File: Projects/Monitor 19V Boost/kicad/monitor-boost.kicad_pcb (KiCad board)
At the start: 2 copper layers, 148 x 118 mm, 47 parts, among them J1 12V IN, J2 19V OUT, Q1 P36NF06, Q2 BD139, Q3 BD140, U1 SG3524

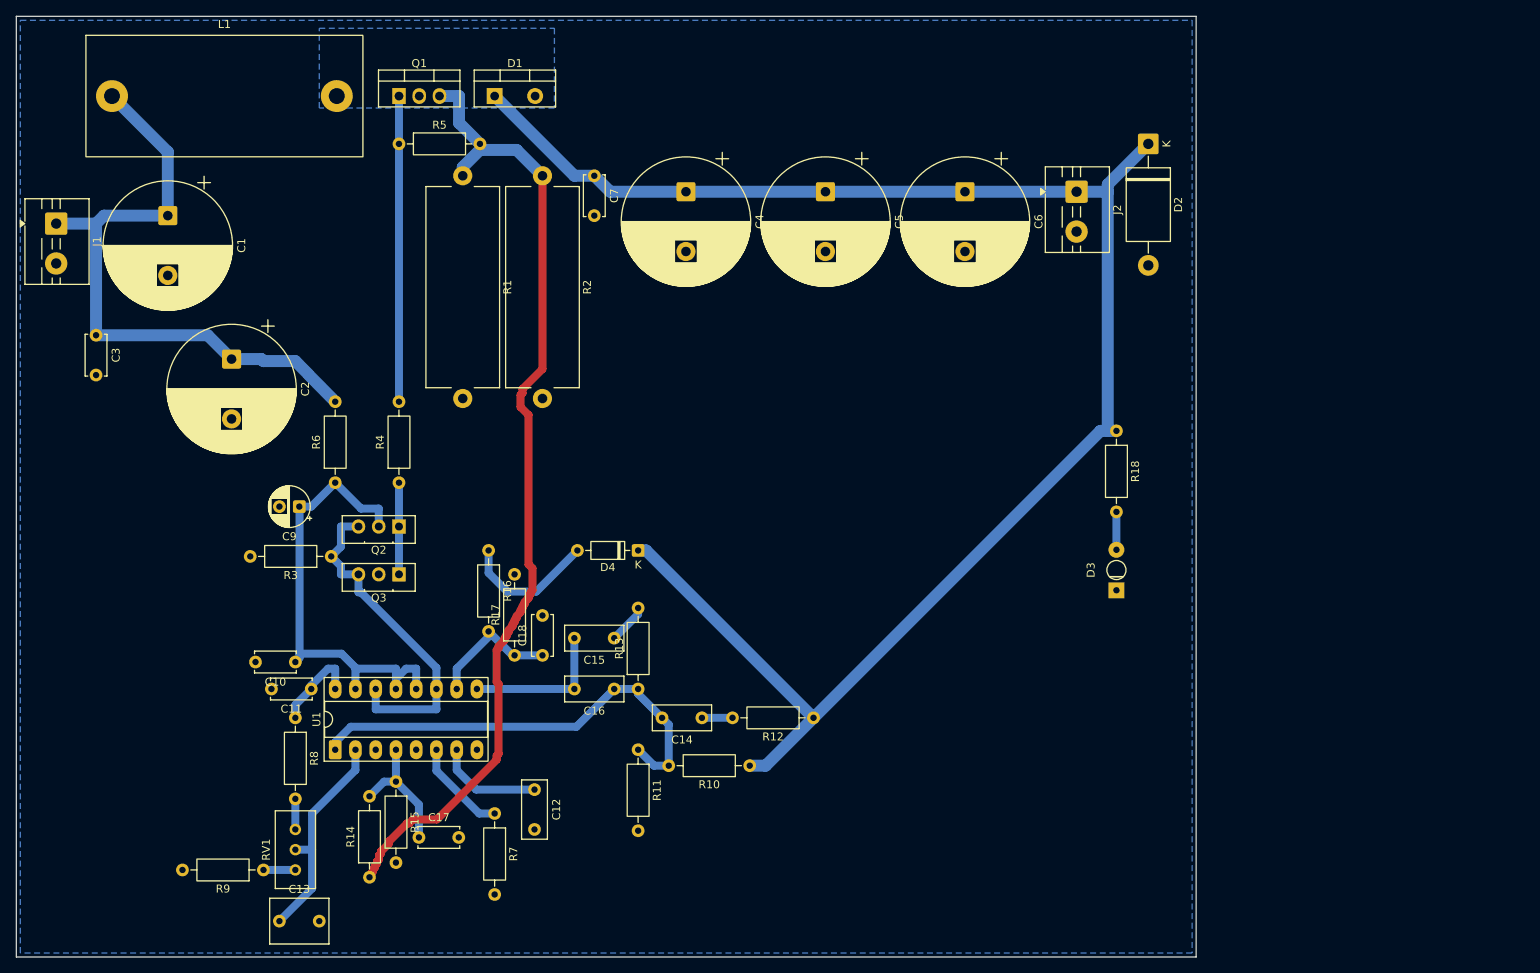
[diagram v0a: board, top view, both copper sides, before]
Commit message: Monitor 19V Boost: hand-drawn layout (before ground fix)
Mads's own redraw of the board. Routes fully on B.Cu with no wire links,
but the VOUT and CS tracks wall the output caps' ground off from the
shunt (hot-loop return ~250 mm round the board edge) and the +12V track
splits C1's minus from the shunt. Kept as the reference for the fix that
follows.
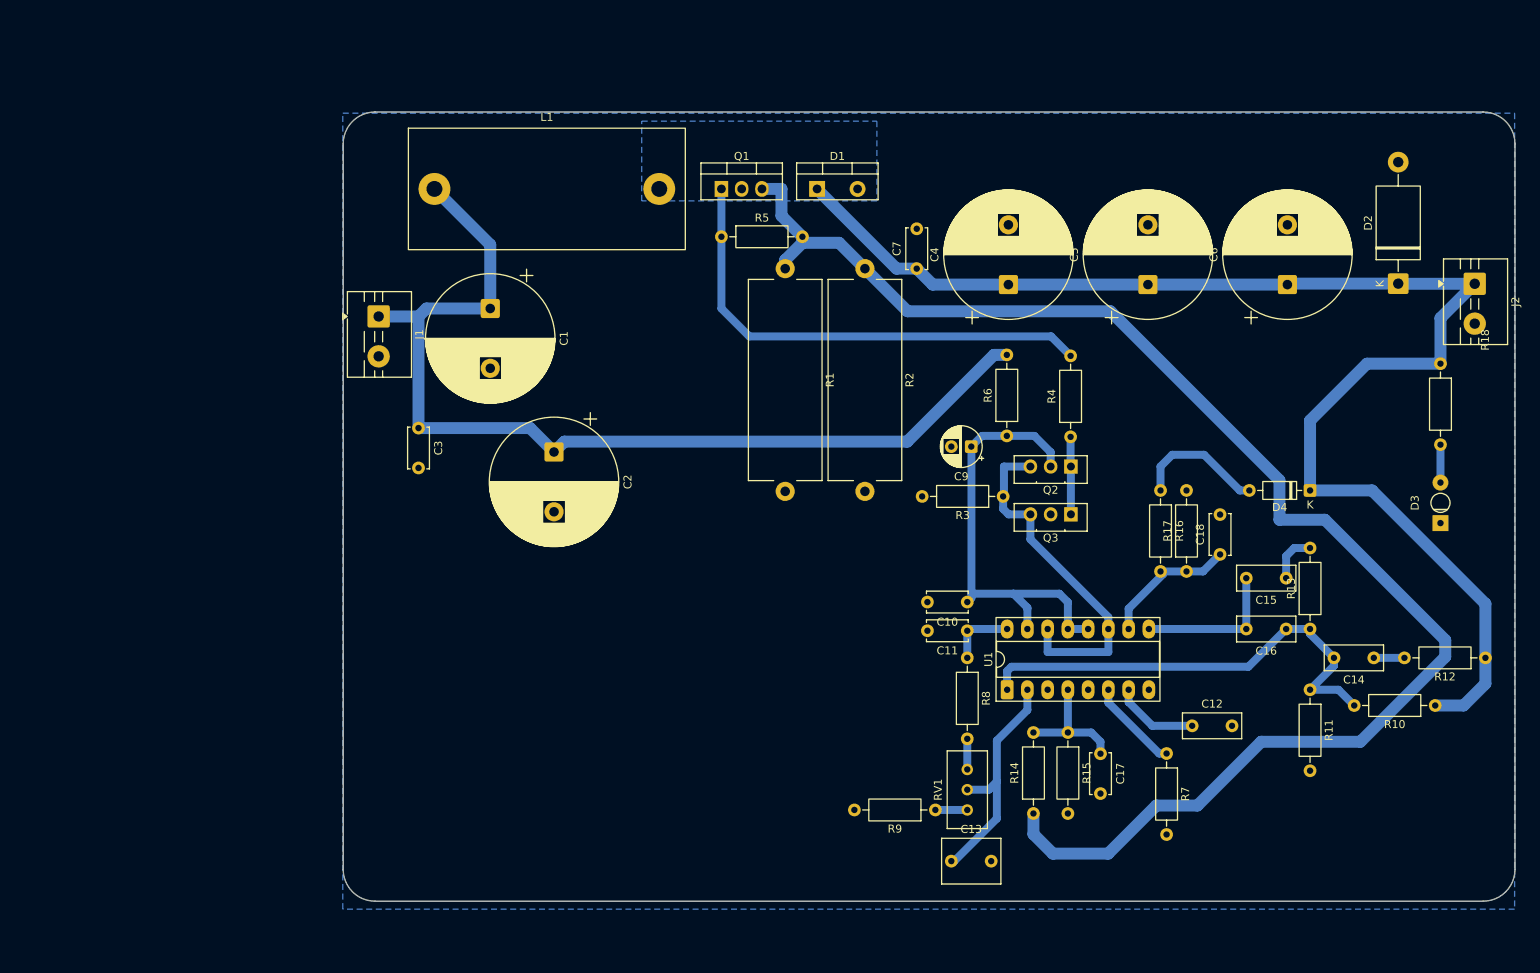
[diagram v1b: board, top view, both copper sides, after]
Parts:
- moved R10 86.3 mm to (198.0, 106.5)
- moved C17 86.1 mm to (156.0, 112.5), turned to -90 degrees
- moved C18 85.9 mm to (171.0, 87.5)
- moved R17 84.9 mm to (166.8, 89.6)
- moved R16 84.6 mm to (163.5, 79.5)
- moved C10 84.6 mm to (139.3, 93.5)
- moved C13 84.6 mm to (137.3, 126.0)
- moved C14 84.6 mm to (190.3, 100.5)
- moved C15 84.6 mm to (179.3, 90.5)
- moved C16 84.6 mm to (179.3, 96.9)
- moved C9 84.6 mm to (139.8, 74.0)
- moved D4 84.6 mm to (182.3, 79.5)
- moved Q2 84.6 mm to (152.3, 76.5)
- moved Q3 84.6 mm to (152.3, 82.5)
- moved R11 84.6 mm to (182.3, 104.5)
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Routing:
- net /CS: track 123.9 -> 186.2 mm
- net +12V: track 79.8 -> 126.4 mm
- net /VOUT: track 214.1 -> 172.8 mm
- net Net-(Q1-G): track 38.3 -> 61.3 mm
- net Net-(U1-REF): track 11.3 -> 8.49 mm
- net Net-(U1-CT): track 13.3 -> 10.8 mm
- net Net-(U1-IN+): track 27.5 -> 29.8 mm
- net Net-(Q2-E): track 11.5 -> 9.74 mm
- net /VCC_F: track 58.2 -> 56.5 mm
- net /DRV: track 42.7 -> 44.2 mm
- net Net-(U1-IN-): track 57.6 -> 59.0 mm
- net Net-(C15-Pad1): track 5.02 -> 6.19 mm
- net /OVP_SD: track 16.7 -> 17.5 mm
- net Net-(U1-RT): track 12.2 -> 11.6 mm
- net /ISENSE: track 16.3 -> 15.8 mm
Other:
- board size 148 x 118 mm -> 147 x 99 mm

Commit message: Monitor 19V Boost: fix the layout's ground topology
Output caps (C4..C6, C7, D2) flipped so their minus pads face the shunt;
VOUT is a pour along the top edge and J2 moves onto it. R4 (gate) and R6
(+12V -> VCC_F) sit right of R2 with their bodies straddling the output
return band; C9 and R3 move out of it. C2 joins C1 in one +12V pour, C3
sits across J1 on an edge stub, Q1 source and the shunt tops are a CS
pour. Two no-track rule areas guard the input and output returns. CS to
R14 is one wire link. VOUT sense runs along the right edge.

Hot-loop return C4- -> shunt: 248 mm / 1.6 mm neck -> 33.5 mm / 7.2 mm.
C1- -> shunt: 132 mm -> 53 mm. DRC: 0 errors, 0 unconnected, no isolated
copper; netlist unchanged. tools/pcb_fix_ground.py reproduces it from the
hand layout.
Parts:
- moved C2 20.4 mm to (97.0, 56.6)
- moved D2 15.2 mm to (193.3, 38.3), turned to -90 degrees
- moved R4 14.5 mm to (142.5, 62.0), turned to 180 degrees
- moved J2 10.5 mm to (202.9, 43.0)
- moved C3 8.66 mm to (62.9, 67.4), turned to 0 degrees
- moved C4 7.50 mm to (144.4, 46.1), turned to -90 degrees
- moved C5 7.50 mm to (161.9, 46.1), turned to -90 degrees
- moved C6 7.50 mm to (179.4, 46.1), turned to -90 degrees
- moved R3 7.10 mm to (147.2, 86.5)
- moved C7 5.00 mm to (132.9, 46.6), turned to -90 degrees
- moved R6 3.18 mm to (142.5, 70.0), turned to 180 degrees
- moved C9 2.86 mm to (142.5, 75.0)
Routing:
- net /CS: track 186.2 -> 91.7 mm
- net +12V: track 126.4 -> 50.3 mm
- net /VOUT: track 172.8 -> 102.6 mm
- net Net-(Q2-E): track 9.74 -> 30.3 mm
- net Net-(Q1-G): track 61.3 -> 43.0 mm
- net /VCC_F: track 56.5 -> 59.5 mm
- net /DRV: track 44.2 -> 41.8 mm
- added copper zone on B.Cu, net +12V
- added copper zone on B.Cu, net /CS
- added copper zone on B.Cu, net /VOUT
